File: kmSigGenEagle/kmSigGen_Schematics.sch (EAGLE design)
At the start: 30 parts, among them IC1 MEGA8-P

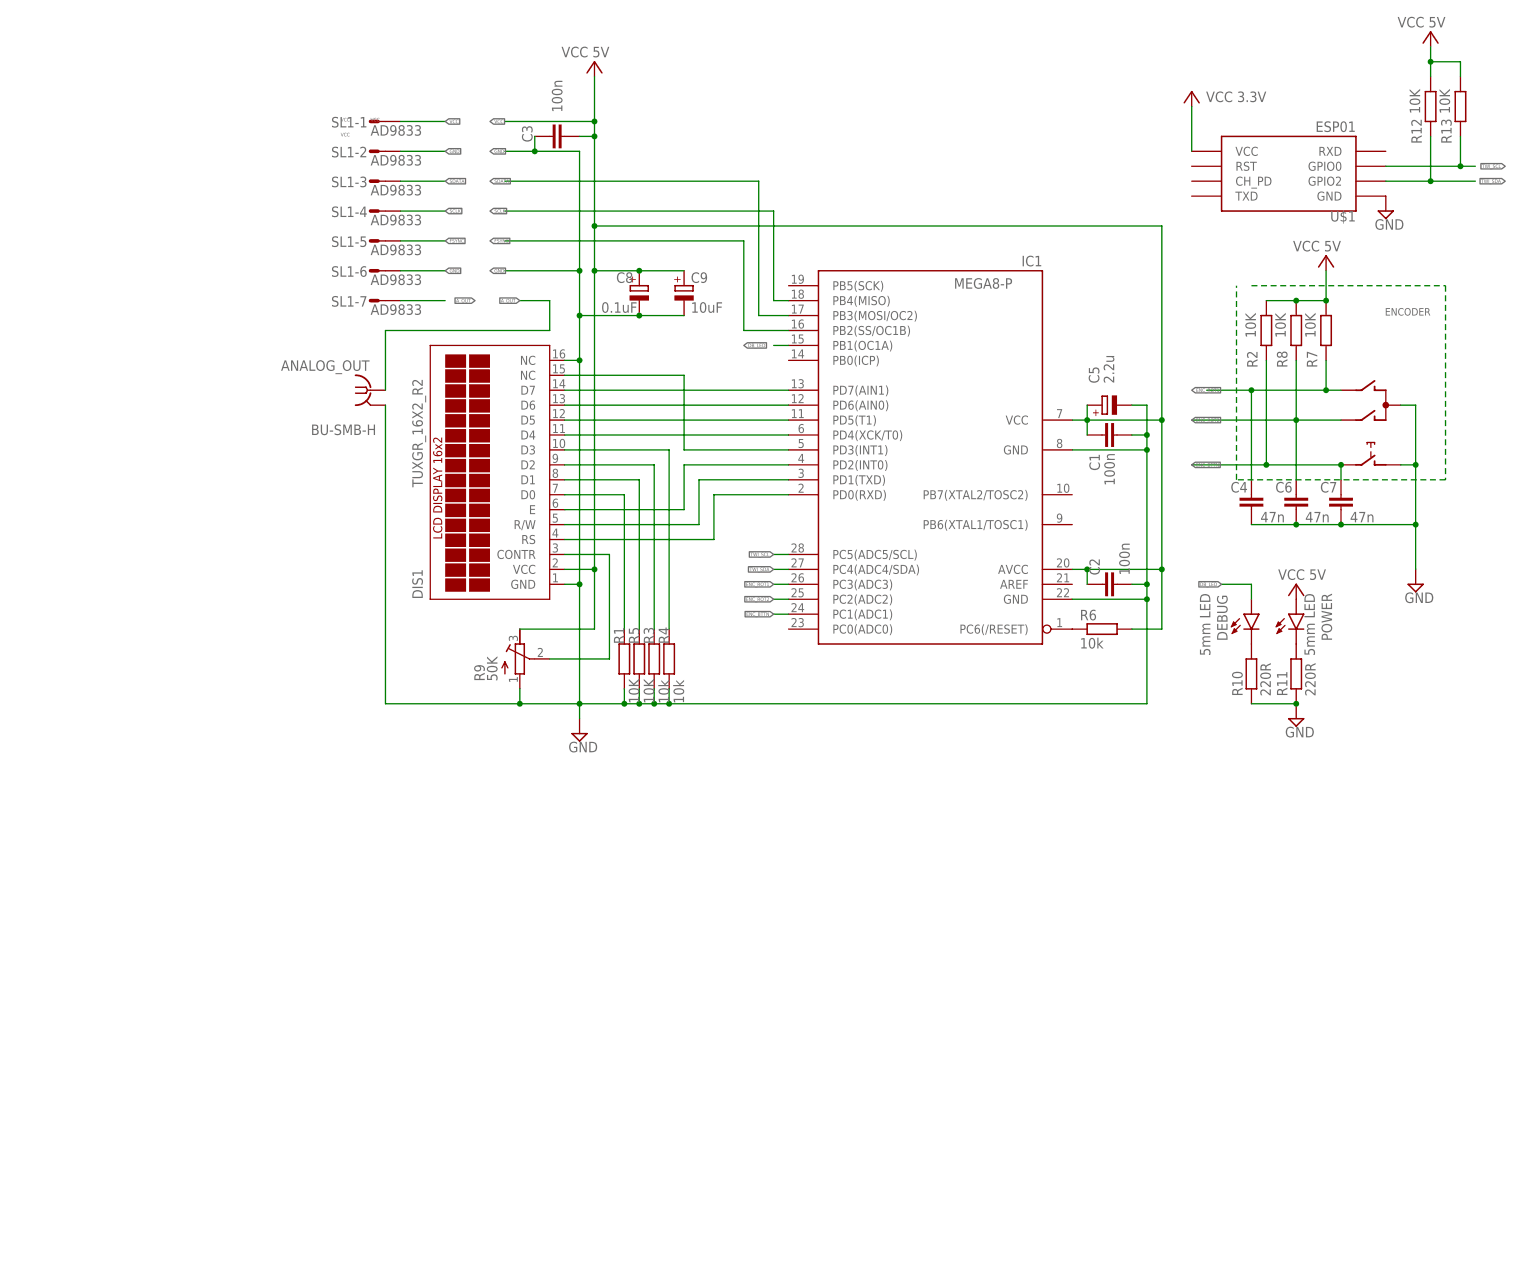
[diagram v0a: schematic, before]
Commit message: Updatech schematics of encoder hardware
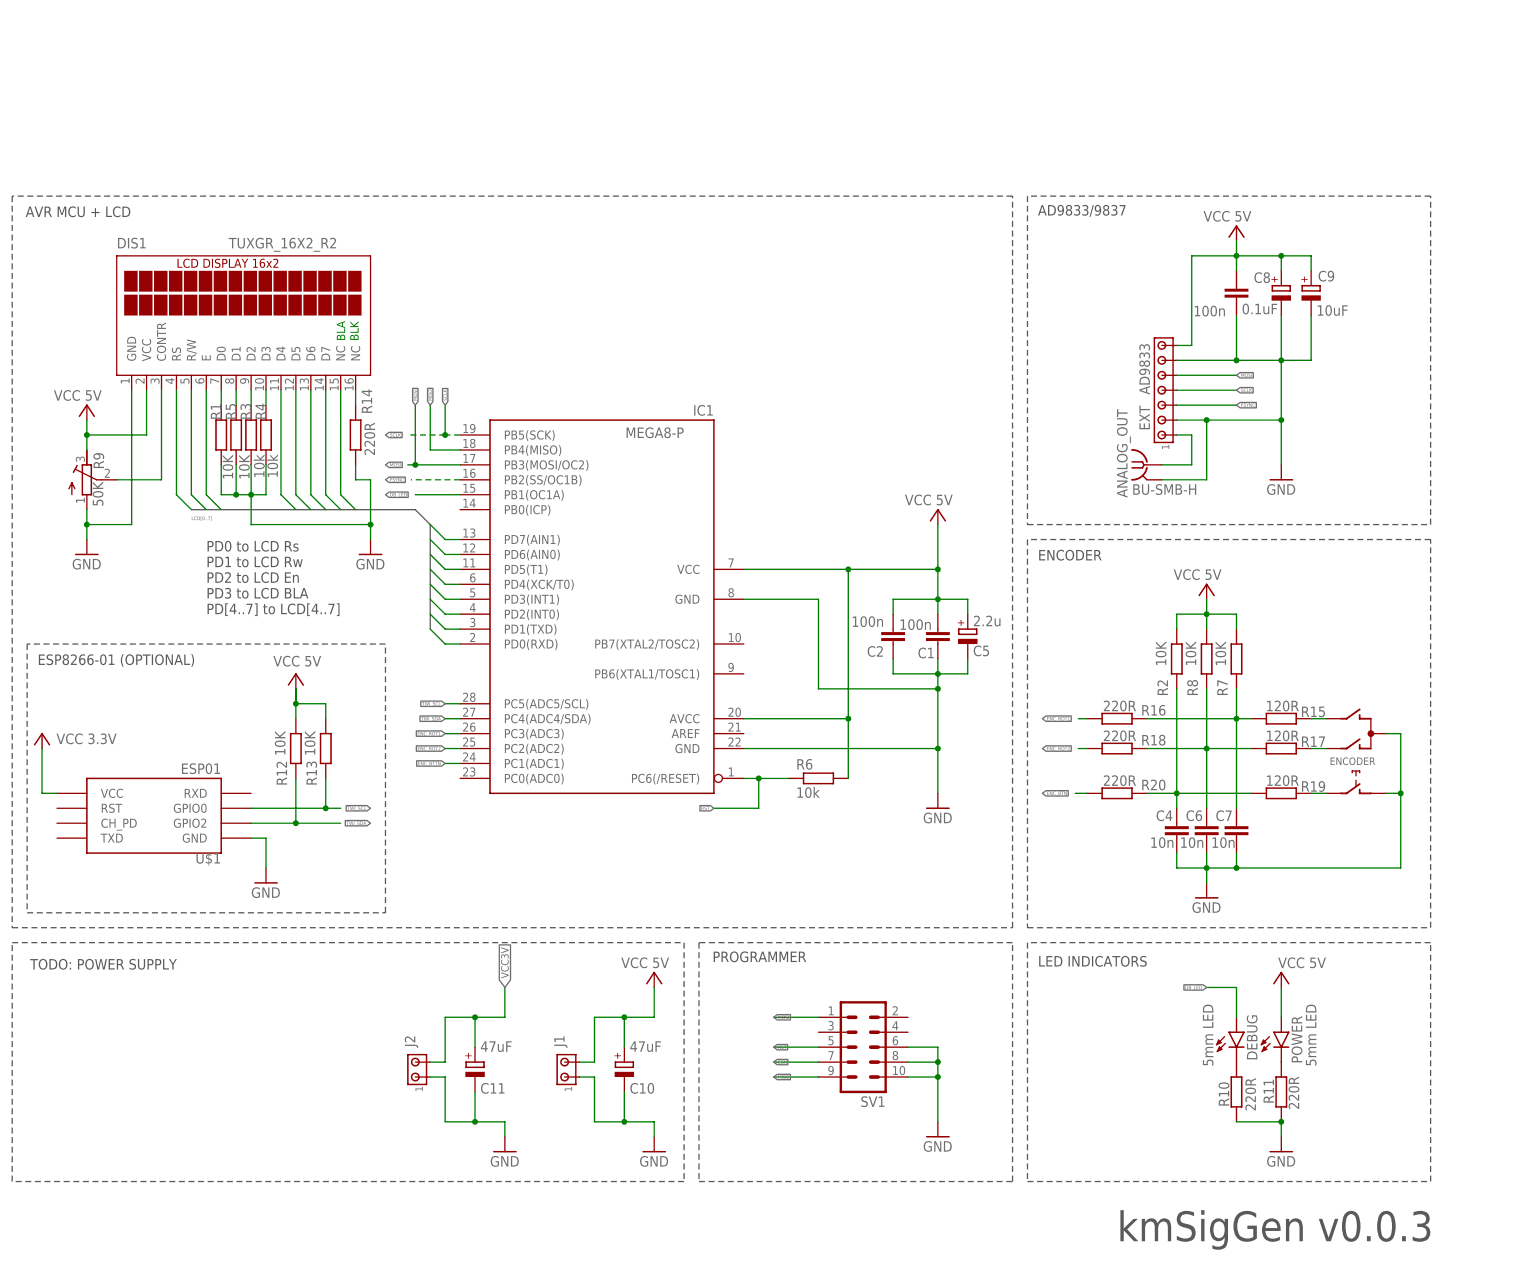
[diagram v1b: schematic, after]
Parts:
- removed SL1: AD9833, con-amp-quick:M07S
- added C10, C11: 47uF, rcl:CPOL-EUB45181B
- added EXT: AD9833, con-amp:MTA07-100
- added J1, J2: (no value), con-amp:MTA02-156
- added R14, R16, R18, R20: 220R, rcl:R-EU_0207/10
- added R15, R17, R19: 120R, rcl:R-EU_0207/10
- added SV1: (no value), con-ml:ML10
- C4, C6, C7: value 47n -> 10n
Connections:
- net LCD_D7 renamed LCD7
- net N$3 renamed LCD6
- net N$4 renamed LCD5
- net N$5 renamed LCD4
- net N$6 renamed LCD3
- net N$7 renamed LCD0
- net N$8 renamed LCD1
- net N$9 renamed LCD2
- removed net A_OUT: ANALOG_OUT.1, SL1-7.S
- removed net SDATA: IC1.PB3(MOSI/OC2), SL1-3.S
- new net ENC_BTN: R20.2
- new net MISO: IC1.PB4(MISO), SV1.9
- new net MOSI: EXT.5, IC1.PB3(MOSI/OC2), SV1.1
- new net N$10: C6.1, R17.2, R18.1, R8.1
- new net N$11: C4.1, R19.2, R2.1, R20.1
- new net N$12: ENCODERG$1.A, R17.1
- new net N$19: ANALOG_OUT.1, EXT.1
- new net N$2: DIS1.NC@2, R14.2
- new net N$8: ENCODERG$1.B, R15.1
- new net N$9: C7.1, R15.2, R16.1, R7.1
- new net RST: IC1.PC6(/RESET), R6.1, SV1.5
- new net SCK: SV1.7
- new net VCC3V: C11.+, J2.2, U$1.VCC
- net ENC_BTTN: no longer C7.1, ENCODERG$2.2, R2.1
- net ENC_ROT1: now also R16.2; no longer C4.1, ENCODERG$1.B, R7.1
- net ENC_ROT2: now also R18.2; no longer C6.1, ENCODERG$1.A, R8.1
- net FSYNC: now also EXT.3; no longer SL1-5.S
- net GND: now also C1.1, C10.-, C11.-, C2.1, EXT.2, EXT.6, J1.1, J2.1, R14.1, SV1.10, SV1.6, SV1.8; no longer C1.2, C2.2, DIS1.NC@2, SL1-2.S, SL1-6.S
- net N$13: now also ENCODERG$2.2, R19.1; no longer IC1.PC6(/RESET), R6.1
- net SCLK: now also EXT.4, IC1.PB5(SCK); no longer IC1.PB4(MISO), SL1-4.S
- net VCC: now also C1.2, C10.+, C2.2, EXT.7, J1.2; no longer C1.1, C2.1, SL1-1.S, U$1.VCC
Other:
- note added: "AD9833/9837"
- note added: "AVR MCU + LCD"
- note added: "BLA"
- note added: "BLK"
- note added: "ENCODER"
- note added: "ESP8266-01 (OPTIONAL)"
- note added: "LED INDICATORS"
- note added: "PD0 to LCD Rs PD1 to LCD Rw PD2 to LCD En PD3 to LCD BLA PD[4..7] to LCD[4..7]"
- note added: "PROGRAMMER"
- note added: "TODO: POWER SUPPLY"
- note added: "kmSigGen v0.0.3"
- moved on the sheet: ANALOG_OUT, C1, C2, C4, C5, C6, C7, C8, C9, DEBUG, DIS1, ENCODER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
